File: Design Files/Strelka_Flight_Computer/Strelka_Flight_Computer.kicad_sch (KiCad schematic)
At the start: 10 parts

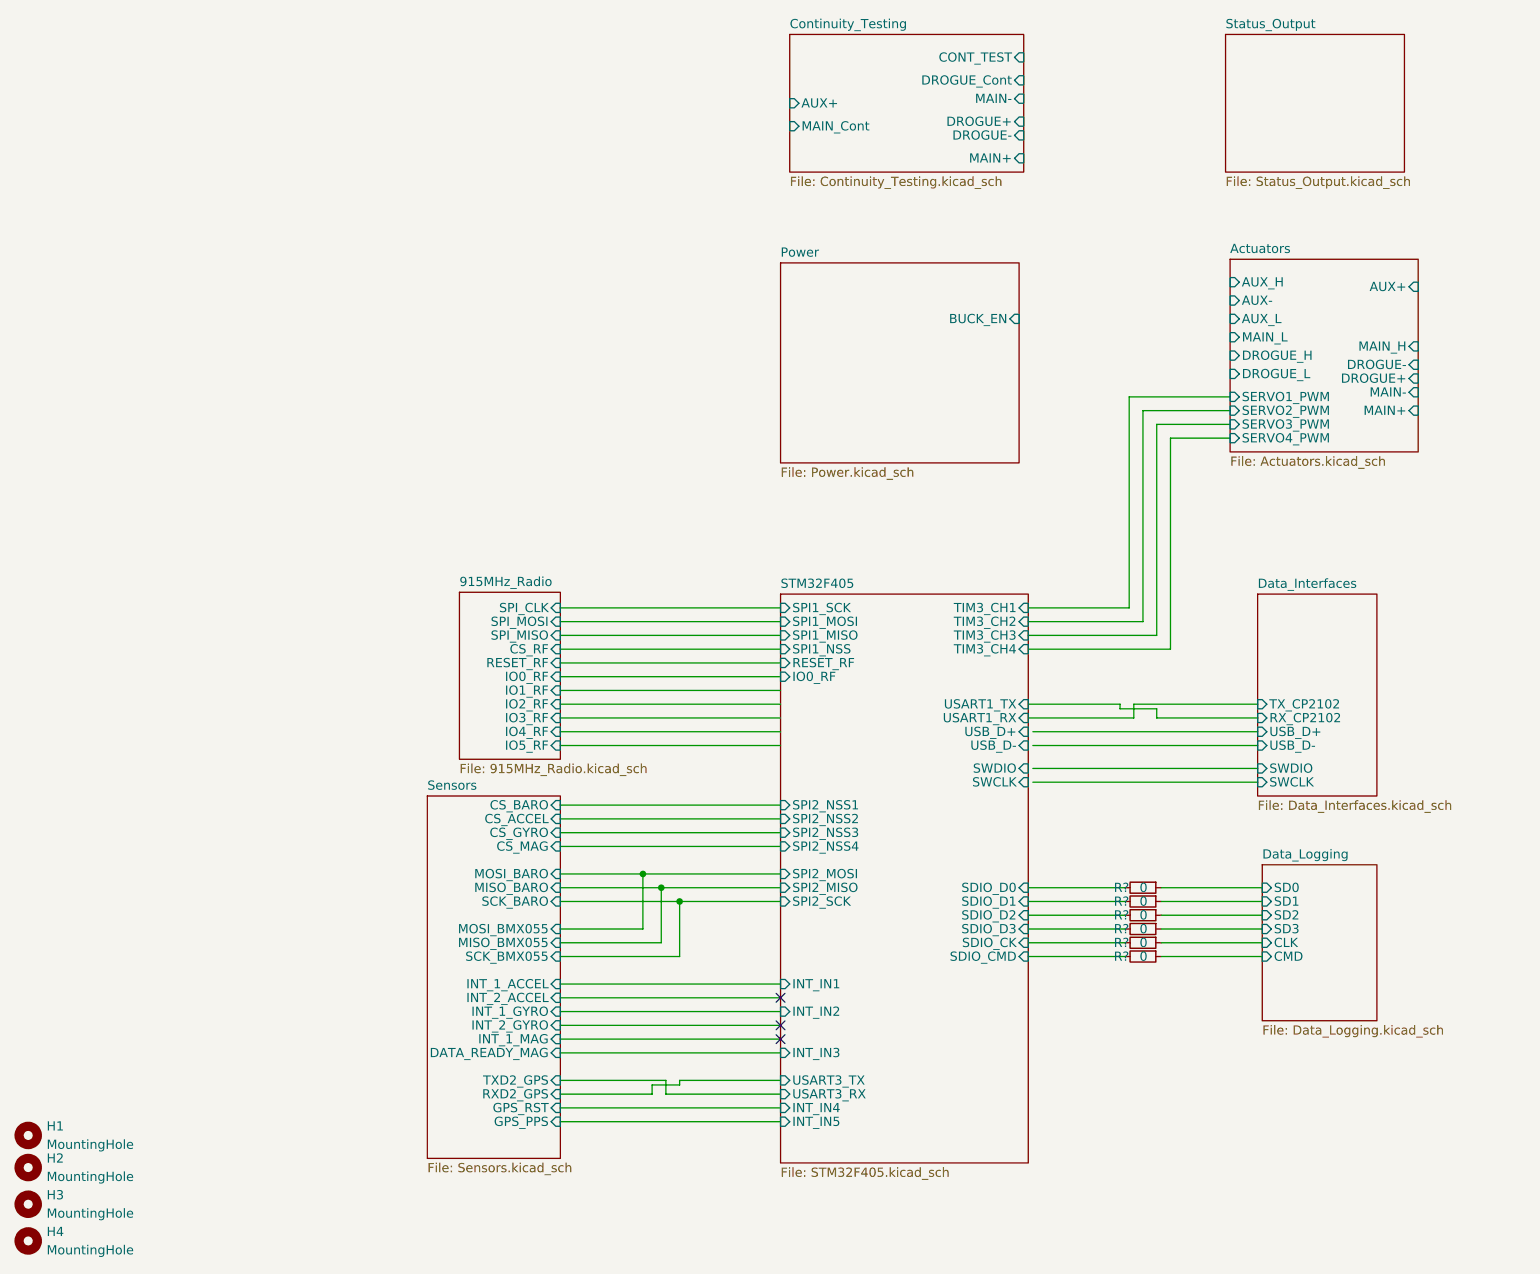
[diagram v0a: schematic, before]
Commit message: Added motor driver to power board
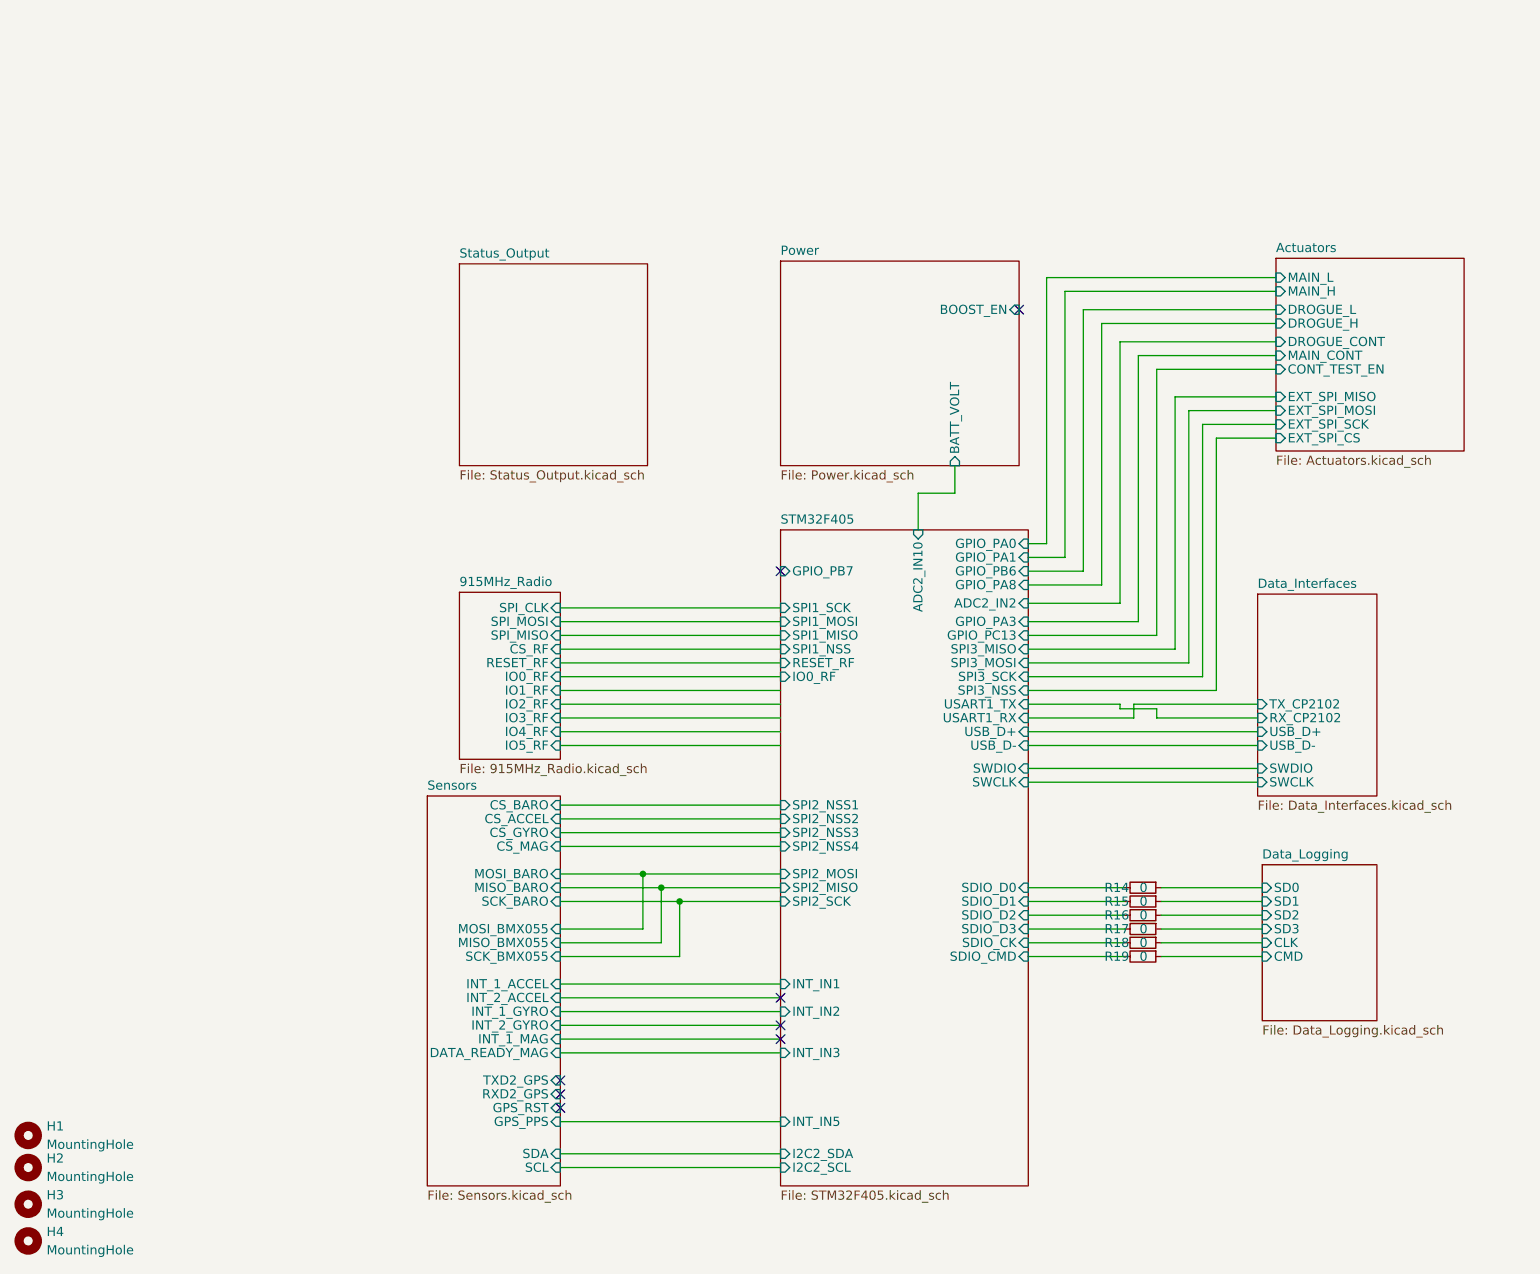
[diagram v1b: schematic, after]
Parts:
- gave numbers to parts that had none: 6
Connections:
- no-connect marks 3 -> 8
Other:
- removed sheet Continuity_Testing
- sheet Actuators ports: added CONT_TEST_EN, DROGUE_CONT, EXT_SPI_CS, EXT_SPI_MISO, EXT_SPI_MOSI, EXT_SPI_SCK, MAIN_CONT; removed AUX+, AUX-, AUX_H, AUX_L, DROGUE+, DROGUE-, MAIN+, MAIN-, SERVO1_PWM, SERVO2_PWM, SERVO3_PWM, SERVO4_PWM
- sheet Power ports: added BATT_VOLT, BOOST_EN; removed BUCK_EN
- sheet STM32F405 ports: added ADC2_IN10, ADC2_IN2, GPIO_PA0, GPIO_PA1, GPIO_PA3, GPIO_PA8, GPIO_PB6, GPIO_PB7, GPIO_PC13, I2C2_SCL, I2C2_SDA, SPI3_MISO, SPI3_MOSI, SPI3_NSS, SPI3_SCK; removed INT_IN4, TIM3_CH1, TIM3_CH2, TIM3_CH3, TIM3_CH4, USART3_RX, USART3_TX
- sheet Sensors ports: added SCL, SDA; removed none

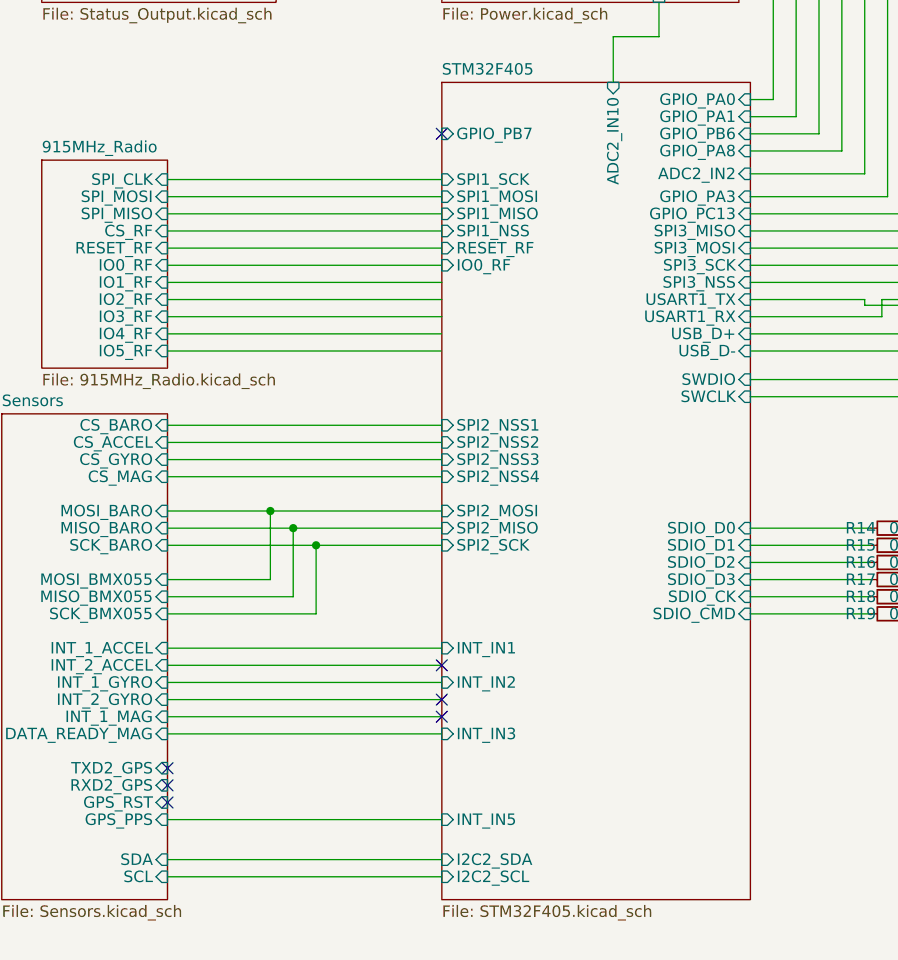
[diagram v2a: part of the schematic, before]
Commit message: Changed boost converter
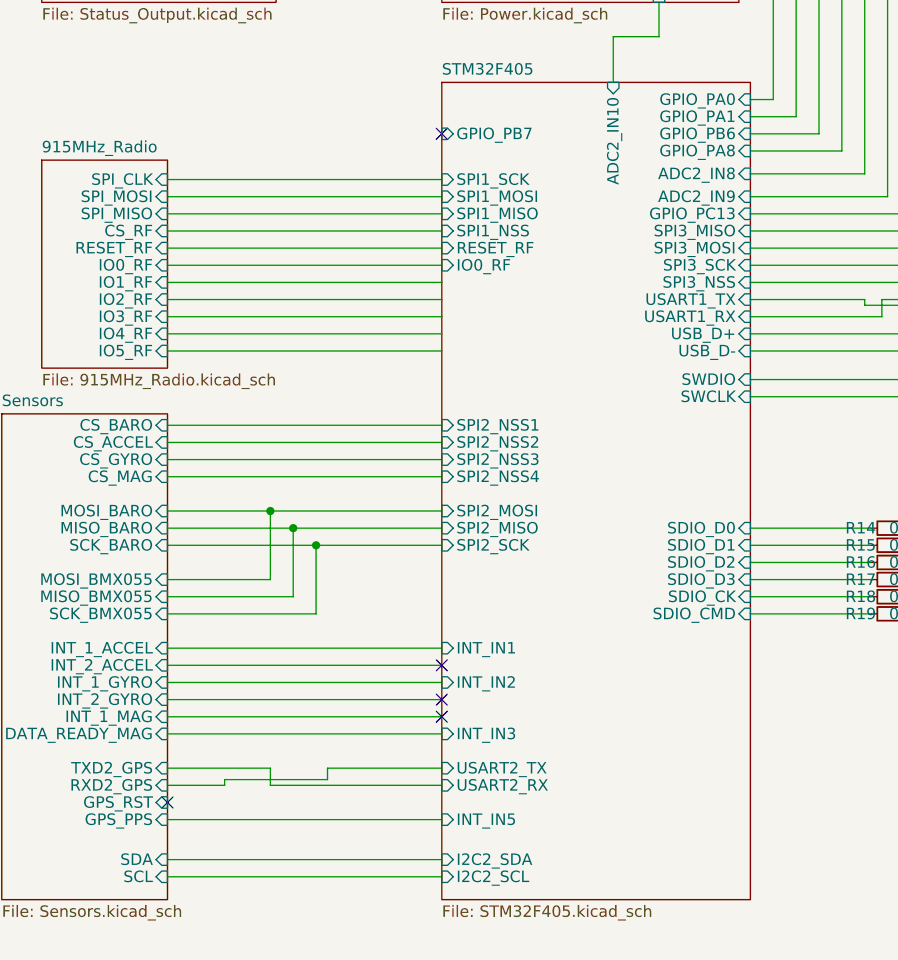
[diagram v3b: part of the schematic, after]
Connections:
- no-connect marks 8 -> 6
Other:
- sheet STM32F405 ports: added ADC2_IN8, ADC2_IN9, USART2_RX, USART2_TX; removed ADC2_IN2, GPIO_PA3

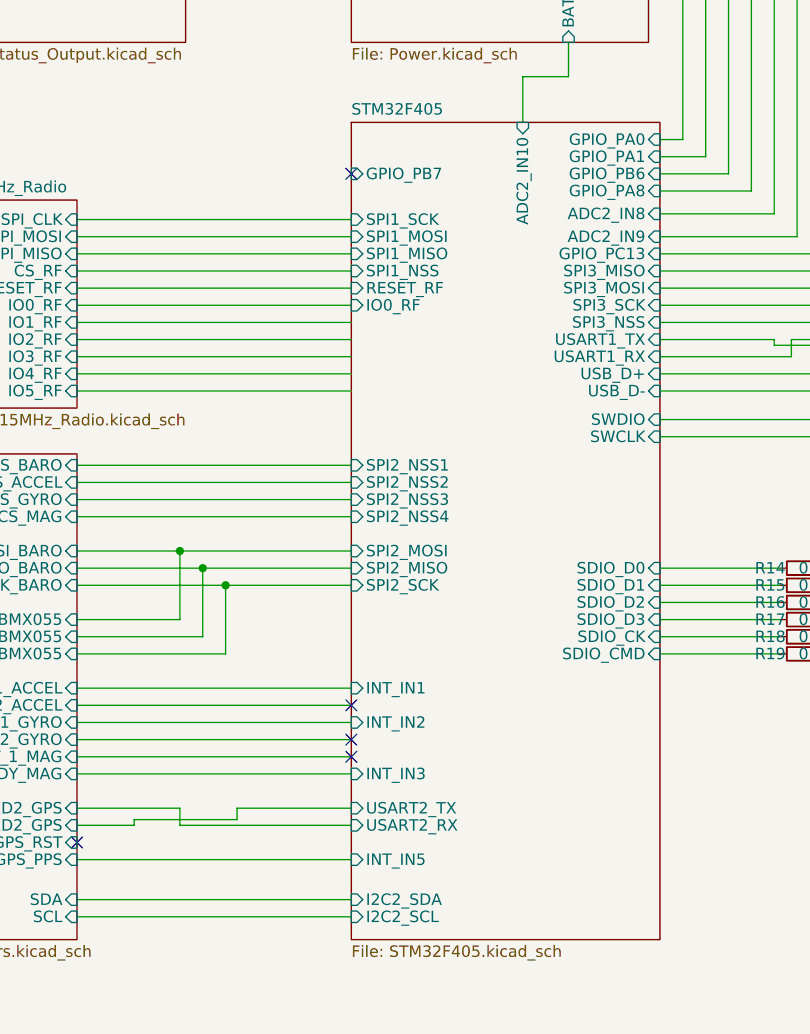
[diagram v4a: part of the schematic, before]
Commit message: Started writing libraries for board functions
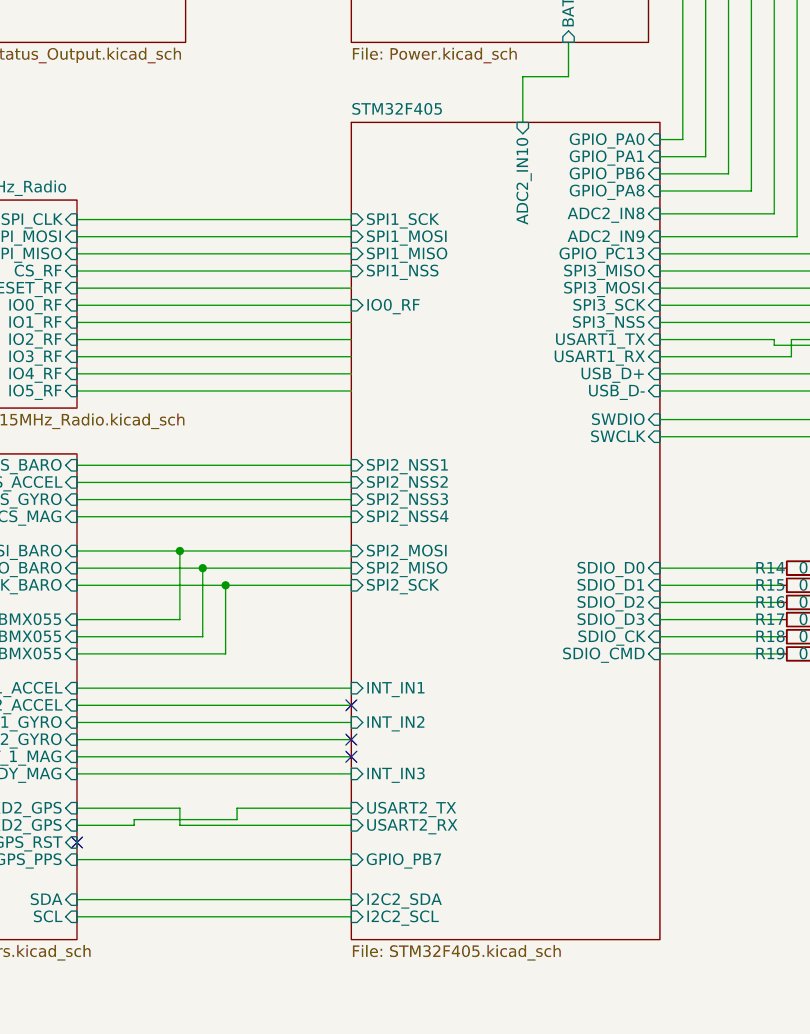
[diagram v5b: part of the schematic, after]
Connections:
- no-connect marks 6 -> 5
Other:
- sheet STM32F405 ports: added none; removed INT_IN5, RESET_RF
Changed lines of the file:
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@@
   (no_connect (at 96.52 166.37))
   (no_connect (at 160.02 55.88))
-  (no_connect (at 127 92.075))
   (no_connect (at 127 154.94))
   (no_connect (at 127 151.13))
@@
       (effects (font (size 1.27 1.27)) (justify right))
     )
-    (pin "RESET_RF" input (at 127 104.775 180)
-      (effects (font (size 1.27 1.27)) (justify left))
-    )
     (pin "IO0_RF" input (at 127 106.68 180)
       (effects (font (size 1.27 1.27)) (justify left))
@@
       (effects (font (size 1.27 1.27)) (justify left))
     )
-    (pin "INT_IN5" input (at 127 168.275 180)
-      (effects (font (size 1.27 1.27)) (justify left))
-    )
     (pin "INT_IN2" input (at 127 153.035 180)
       (effects (font (size 1.27 1.27)) (justify left))
@@
       (effects (font (size 1.27 1.27)) (justify right))
     )
-    (pin "GPIO_PB7" input (at 127 92.075 180)
-      (effects (font (size 1.27 1.27)) (justify left))
-    )
+    (pin "GPIO_PB7" input (at 127 168.275 180)
+      (effects (font (size 1.27 1.27)) (justify left))
+    )
